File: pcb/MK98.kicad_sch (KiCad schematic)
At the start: 53 parts, among them J1 USB C, J3 Conn_01x05_Pin, J4 OLED-128x32, Q1 AO3401A, Q2 BSS138, U1 AP2112K-3.3, U2 SN74LV1T125DBV, U3 USBLC6-2SC6, U4 STM32F405RGTx, Y1 8Mhz

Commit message: add the GPIO for extra feature
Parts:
- added J5: Conn_01x04, Connector_JST:JST_SH_SM04B-SRSS-TB_1x04-1MP_P1.00mm_Horizontal, symbol Connector_Generic:Conn_01x04
- added J6, J7: Conn_01x03, Connector_JST:JST_SH_SM03B-SRSS-TB_1x03-1MP_P1.00mm_Horizontal, symbol Connector_Generic:Conn_01x03
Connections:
- net at U4.10 (PC2): now also J5.3 (Pin_3)
- net at U4.11 (PC3): now also J5.4 (Pin_4)
- net at U4.14 (PA0): now also J6.1 (Pin_1)
- net at U4.15 (PA1): now also J6.2 (Pin_2)
- net at U4.16 (PA2): now also J6.3 (Pin_3)
- net at U4.20 (PA4): now also J7.1 (Pin_1)
- net at U4.21 (PA5): now also J7.2 (Pin_2)
- net at U4.22 (PA6): now also J7.3 (Pin_3)
- net at U4.8 (PC0): now also J5.1 (Pin_1)
- net at U4.9 (PC1): now also J5.2 (Pin_2)
- no-connect marks 26 -> 16
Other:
- note added: "GPIO Extender"

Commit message: Normalize line endings to LF
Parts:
- C102: LCSC (none) -> C19666; LCSCC C14663 -> (none)
- C103: LCSC (none) -> C19702
- C108, C109: footprint Capacitor_Tantalum_SMD:CP_EIA-3216-12_Kemet-S -> Capacitor_Tantalum_SMD:CP_EIA-3528-21_Kemet-B; LCSC C116270 -> C7207
- C114: LCSC C14663 -> C19666
- C120: LCSC (none) -> C100042
- C125: value 100n -> 100nf; LCSC (none) -> C14663
- C132: LCSC (none) -> C23630
- C99: LCCSC C14663 -> (none); LCSC (none) -> C14663
- F1: footprint Fuse:Fuse_0603_1608Metric -> Fuse:Fuse_1206_3216Metric; LCSC C210357 -> C89653
- J5: LCSC (none) -> C5329994
- J6, J7: LCSC (none) -> C160403
- Q1: LCSC (none) -> C5379091
- Q2: LCSC (none) -> C3015220
- R1, R2: LCSC (none) -> C14675
- R10, R11: LCSC (none) -> C98220
- R3: LCSC (none) -> C22935
- R8, R9: LCSC (none) -> C2907044

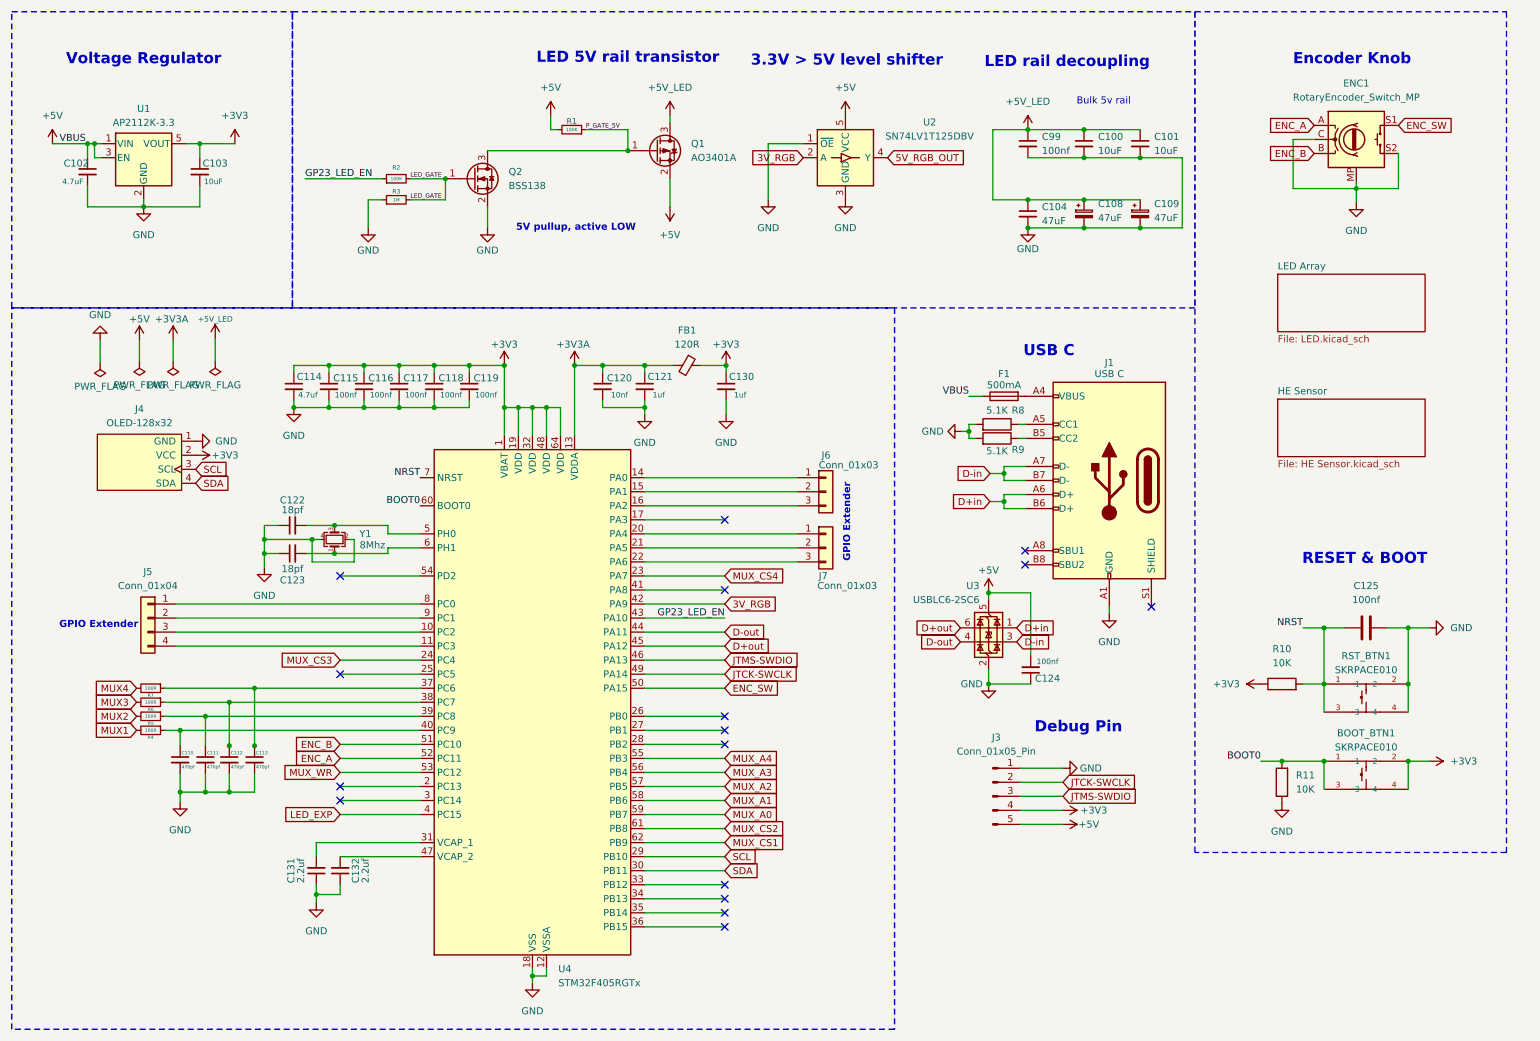
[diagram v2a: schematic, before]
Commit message: adding flash memory to store user config
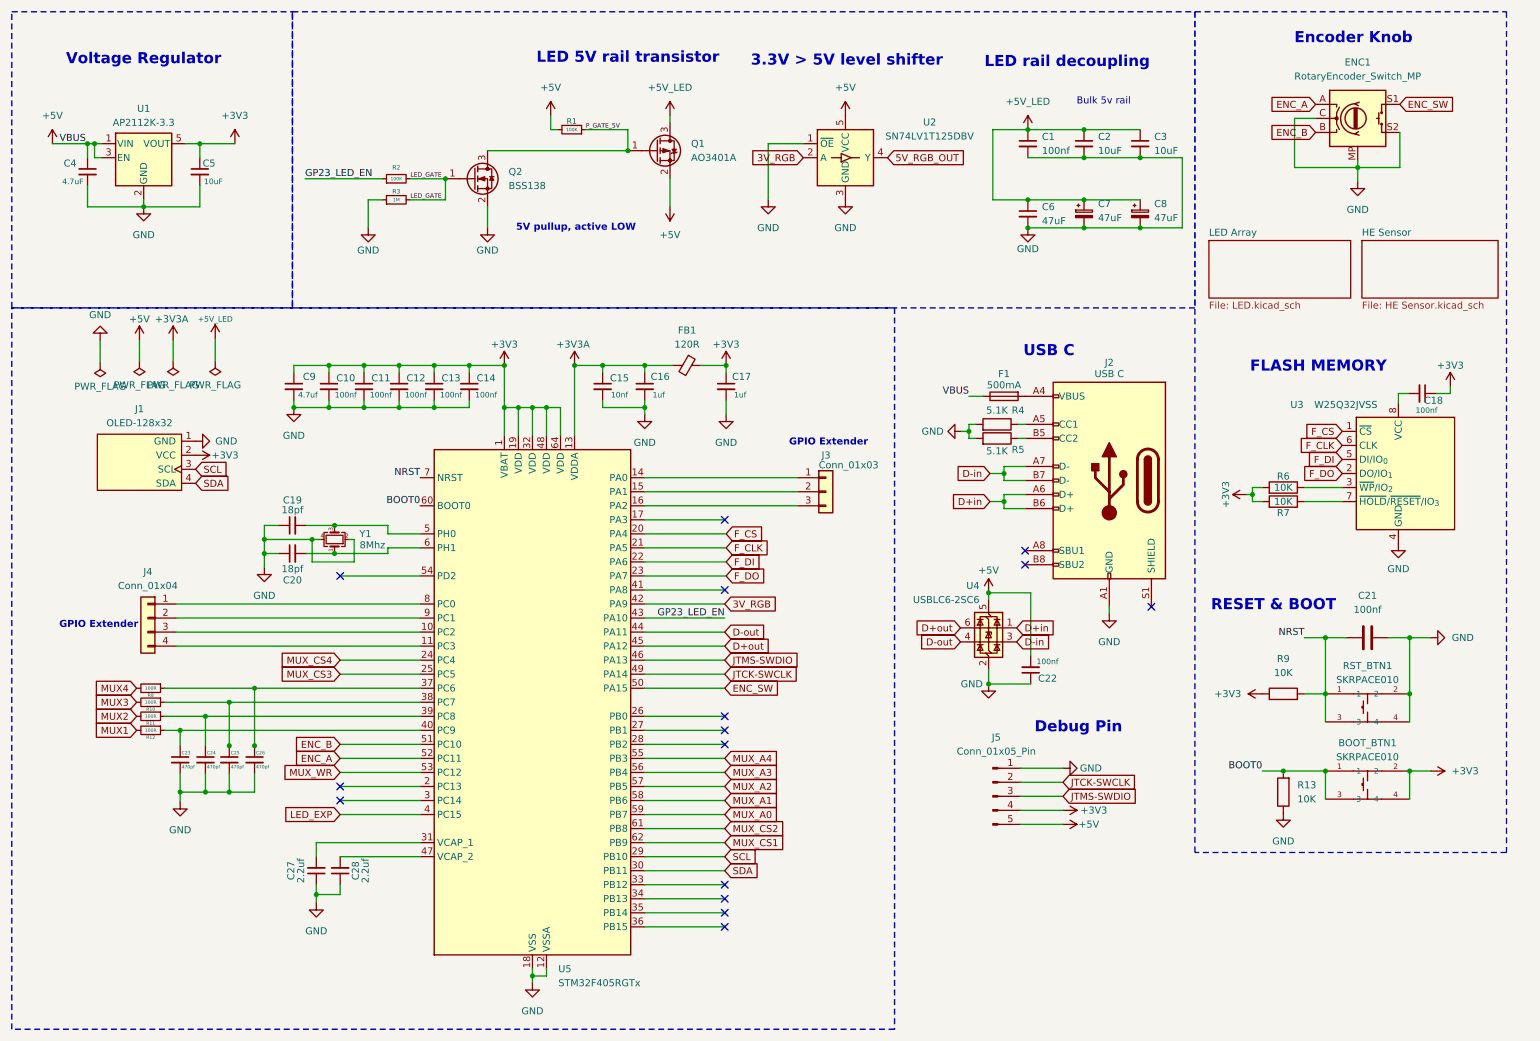
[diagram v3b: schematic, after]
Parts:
- removed J7: Conn_01x03, Connector_JST:JST_SH_SM03B-SRSS-TB_1x03-1MP_P1.00mm_Horizontal, symbol Connector_Generic:Conn_01x03
- added C18: 100nf, Capacitor_SMD:C_0603_1608Metric, symbol Device:C_Small
- added R6, R7: 10K, Resistor_SMD:R_0603_1608Metric, symbol Device:R
- added U3: W25Q32JVSS, Package_SO:SOIC-8_5.3x5.3mm_P1.27mm, symbol Memory_Flash:W25Q32JVSS
- R13: renamed from R11; footprint Resistor_SMD:R_0402_1005Metric_Pad0.72x0.64mm_HandSolder -> Resistor_SMD:R_0603_1608Metric
- R9: renamed from R10; footprint Resistor_SMD:R_0402_1005Metric_Pad0.72x0.64mm_HandSolder -> Resistor_SMD:R_0603_1608Metric
- renumbered C99 to C1, C115 to C10, C116 to C11, C117 to C12, C118 to C13, C119 to C14, C120 to C15, C121 to C16, C130 to C17, C122 to C19, C100 to C2, C123 to C20, C125 to C21, C124 to C22, C110 to C23, C111 to C24, C112 to C25, C113 to C26, C131 to C27, C132 to C28, C101 to C3, C102 to C4, C103 to C5, C104 to C6, C108 to C7, C109 to C8, C114 to C9, J4 to J1, J1 to J2, J6 to J3, J5 to J4, J3 to J5, R6 to R10, R5 to R11, R4 to R12, R8 to R4, R9 to R5, R7 to R8, U3 to U4, U4 to U5
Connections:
- net +3V3: now also C18.1, R6.2, R7.2
- net GND: now also U3.4 (GND)
- net MUX_CS3: now also U5.25 (PC5); no longer U5.24 (PC4)
- net MUX_CS4: now also U5.24 (PC4); no longer U5.23 (PA7)
- net F_CS: now reaches U5.20 (PA4)
- net F_CS: now also U3.1 (~{CS})
- net F_CLK: now reaches U5.21 (PA5)
- net F_CLK: now also U3.6 (CLK)
- net F_DI: now reaches U5.22 (PA6)
- net F_DI: now also U3.5 (DI/IO_{0})
- new net: R7.1, U3.7 (~{HOLD}/~{RESET}/IO_{3})
- new net: R6.1, U3.3 (~{WP}/IO_{2})
- new net: C18.2, U3.8 (VCC)
- new net F_DO: U3.2 (DO/IO_{1}), U5.23 (PA7)
- no-connect marks 16 -> 15
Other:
- note added: "FLASH MEMORY"
- moved on the sheet: BOOT_BTN1, C21, ENC1, R13, R9, RST_BTN1
